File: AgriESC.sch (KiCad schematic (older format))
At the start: 131 parts, among them J1 SUPPLY, J10 GPIO, J11 USB_OTG, J12 HALL_ENC, J2 PH_A, J3 PH_B, J4 PH_C, J6 COMM, J7 SERVO, J8 CAN, J9 SWD, SW1 SW_SPDT, U1 FDMS7698, U10 STM32F405RGT6, U11 DRV8303, U12 TJA1051TK-3, U13 LMR16006YQ, U14 MCP1700-3302E_SOT23, U15 MCP1700-3302E_SOT23, U2 FDMS7698, U3 FDMS7698, U4 FDMS7698, U5 FDMS7698, U6 FDMS7698, U7 MAX9920, U8 MAX9920, U9 MAX9920, Y1 8M Resonator

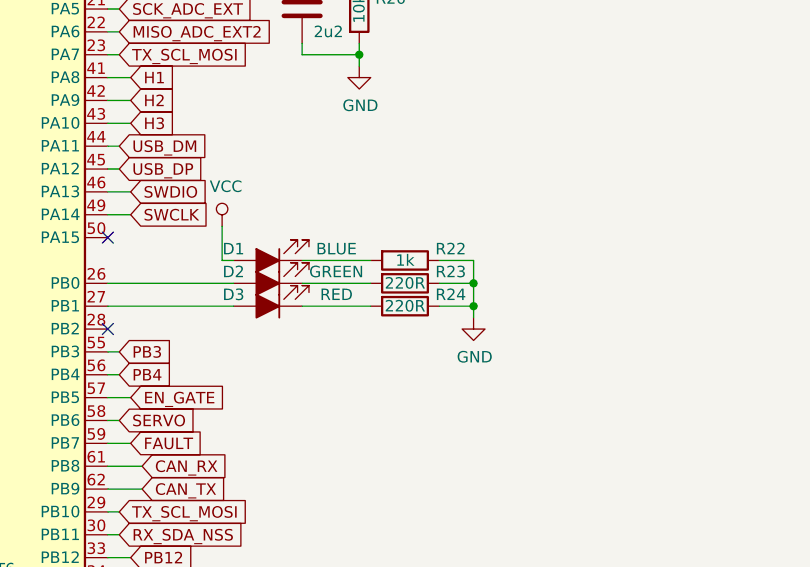
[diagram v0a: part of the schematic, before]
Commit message: Updated LED resistors
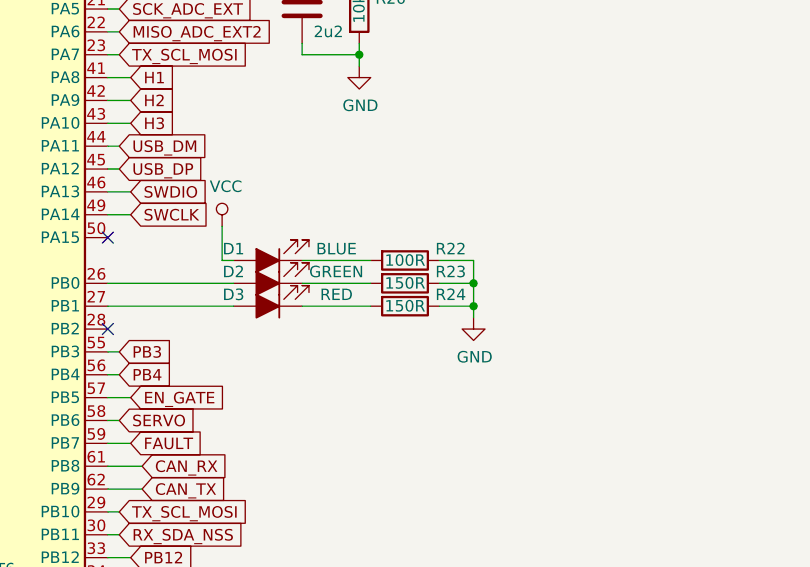
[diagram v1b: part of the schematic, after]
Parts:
- R22: value 1k -> 100R
- R23, R24: value 220R -> 150R
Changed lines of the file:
@@
 P 16400 7350
 F 0 "R22" V 16350 7550 50  0000 C CNN
-F 1 "1k" V 16400 7350 50  0000 C CNN
+F 1 "100R" V 16400 7350 50  0000 C CNN
 F 2 "Resistor_SMD:R_0603_1608Metric_Pad1.05x0.95mm_HandSolder" V 16330 7350 50  0001 C CNN
 F 3 "~" H 16400 7350 50  0001 C CNN
@@
 P 16400 7450
 F 0 "R23" V 16350 7650 50  0000 C CNN
-F 1 "220R" V 16400 7450 50  0000 C CNN
+F 1 "150R" V 16400 7450 50  0000 C CNN
 F 2 "Resistor_SMD:R_0603_1608Metric_Pad1.05x0.95mm_HandSolder" V 16330 7450 50  0001 C CNN
 F 3 "~" H 16400 7450 50  0001 C CNN
@@
 P 16400 7550
 F 0 "R24" V 16350 7750 50  0000 C CNN
-F 1 "220R" V 16400 7550 50  0000 C CNN
+F 1 "150R" V 16400 7550 50  0000 C CNN
 F 2 "Resistor_SMD:R_0603_1608Metric_Pad1.05x0.95mm_HandSolder" V 16330 7550 50  0001 C CNN
 F 3 "~" H 16400 7550 50  0001 C CNN

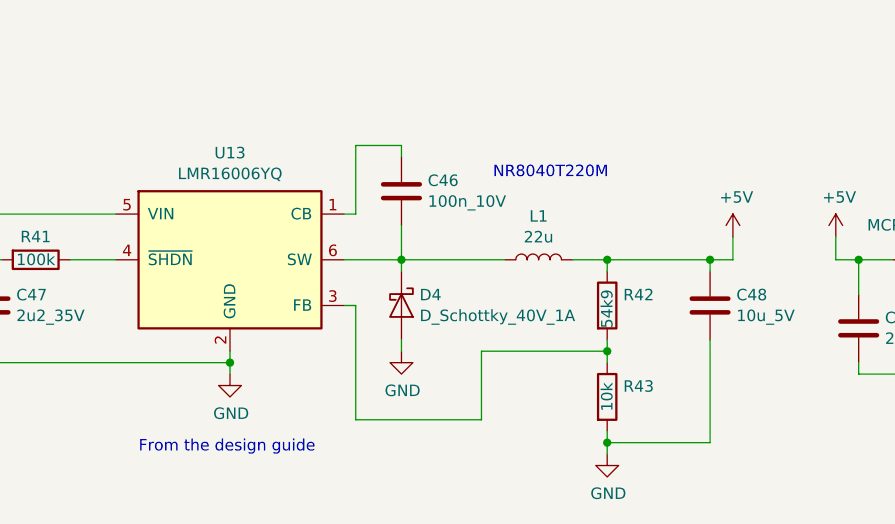
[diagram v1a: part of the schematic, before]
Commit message: Updated LMR16006YQ to fixed 5V version, removed feedback resistors
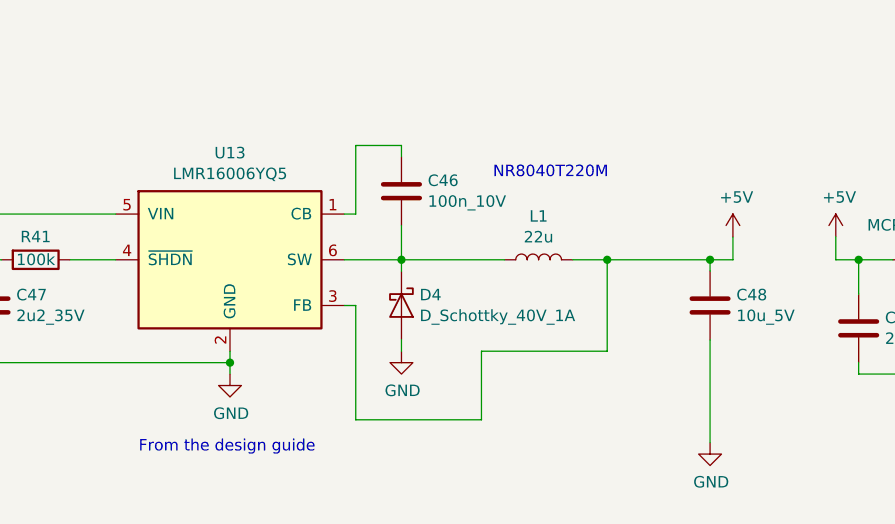
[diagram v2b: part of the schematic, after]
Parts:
- removed R42: 54k9, Resistor_SMD:R_0603_1608Metric_Pad1.05x0.95mm_HandSolder, symbol Device:R
- removed R43: 10k, Resistor_SMD:R_0603_1608Metric_Pad1.05x0.95mm_HandSolder, symbol Device:R
- U13: value LMR16006YQ -> LMR16006YQ5
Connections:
- net +5V: now also U13.3 (FB)
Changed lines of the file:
@@
 P 8700 13200
 F 0 "U13" H 8700 13667 50  0000 C CNN
-F 1 "LMR16006YQ" H 8700 13576 50  0000 C CNN
+F 1 "LMR16006YQ5" H 8700 13576 50  0000 C CNN
 F 2 "Package_TO_SOT_SMD:SOT-23-6" H 8700 12700 50  0001 C CIN
 F 3 "http://www.ti.com/lit/ds/symlink/lmr16006y-q1.pdf" H 8300 13650 50  0001 C CNN
@@
 	9450 13550 9450 13600
 $Comp
-L Device:R R42
-U 1 1 5DD532F3
-P 10350 13400
-F 0 "R42" H 10420 13446 50  0000 L CNN
-F 1 "54k9" V 10350 13300 50  0000 L CNN
-F 2 "Resistor_SMD:R_0603_1608Metric_Pad1.05x0.95mm_HandSolder" V 10280 13400 50  0001 C CNN
-F 3 "~" H 10350 13400 50  0001 C CNN
-	1    10350 13400
-	1    0    0    -1
-$EndComp
-$Comp
-L Device:R R43
-U 1 1 5DD53451
-P 10350 13800
-F 0 "R43" H 10420 13846 50  0000 L CNN
-F 1 "10k" V 10350 13800 50  0000 C CNN
-F 2 "Resistor_SMD:R_0603_1608Metric_Pad1.05x0.95mm_HandSolder" V 10280 13800 50  0001 C CNN
-F 3 "~" H 10350 13800 50  0001 C CNN
-	1    10350 13800
-	1    0    0    -1
-$EndComp
-$Comp
 L power:GND #PWR069
 U 1 1 5DD5355D
-P 10350 14050
-F 0 "#PWR069" H 10350 13800 50  0001 C CNN
-F 1 "GND" H 10355 13877 50  0000 C CNN
-F 2 "" H 10350 14050 50  0001 C CNN
-F 3 "" H 10350 14050 50  0001 C CNN
-	1    10350 14050
-	1    0    0    -1
-$EndComp
-Wire Wire Line
-	10350 13550 10350 13600
-Wire Wire Line
-	10350 13250 10350 13200
+P 10800 14000
+F 0 "#PWR069" H 10800 13750 50  0001 C CNN
+F 1 "GND" H 10805 13827 50  0000 C CNN
+F 2 "" H 10800 14000 50  0001 C CNN
+F 3 "" H 10800 14000 50  0001 C CNN
+	1    10800 14000
+	1    0    0    -1
+$EndComp
 Wire Wire Line
 	10350 13200 10200 13200
@@
 Wire Wire Line
 	9800 13600 10350 13600
-Connection ~ 10350 13600
-Wire Wire Line
-	10350 13600 10350 13650
 $Comp
 L Device:C C48
@@
 Wire Wire Line
 	10800 13550 10800 14000
-Wire Wire Line
-	10350 13950 10350 14000
-Wire Wire Line
-	10800 14000 10350 14000
-Connection ~ 10350 14000
-Wire Wire Line
-	10350 14000 10350 14050
 Wire Wire Line
 	10800 13200 10900 13200
@@
 Text Label 10050 10500 2    50   ~ 0
 HALL_POWER
+Wire Wire Line
+	10350 13200 10350 13600
 $EndSCHEMATC

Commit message: Updated USB footprint
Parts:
- J11: footprint AgriESC:CONN-10118194-0001LF-FCI2 -> AgriESC:CONN-10118194-0001LF-FCI3
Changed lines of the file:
@@
 F 0 "J11" H 15655 10267 50  0000 C CNN
 F 1 "USB_OTG" H 15655 10176 50  0000 C CNN
-F 2 "AgriESC:CONN-10118194-0001LF-FCI2" H 15750 9750 50  0001 C CNN
+F 2 "AgriESC:CONN-10118194-0001LF-FCI3" H 15750 9750 50  0001 C CNN
 F 3 " ~" H 15750 9750 50  0001 C CNN
 	1    15600 9800

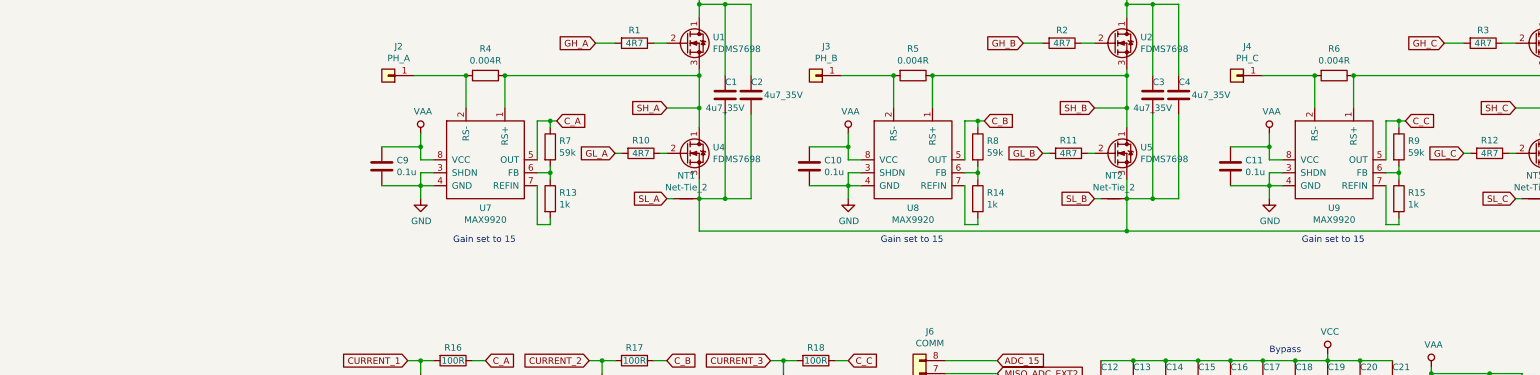
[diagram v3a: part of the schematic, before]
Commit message: Added new MAX9920 VREFIN
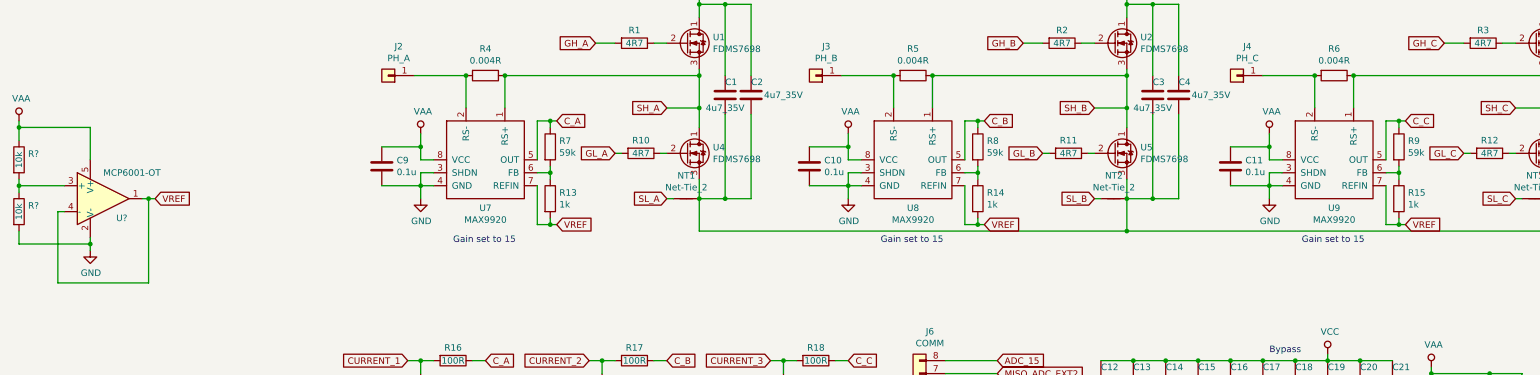
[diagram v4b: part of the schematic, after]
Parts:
- added R? (x2): 10k, Resistor_SMD:R_0603_1608Metric_Pad1.05x0.95mm_HandSolder, symbol Device:R
- added U?: MCP6001-OT, Package_TO_SOT_SMD:SOT-23-5, symbol Amplifier_Operational:MCP6001-OT
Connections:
- net GND: now also R?.2, U?.2 (V-)
- net VAA: now also R?.1, U?.5 (V+)
- net VREF: now reaches R13.2, U7.7 (REFIN)
- net VREF: now also R14.2, R15.2, U8.7 (REFIN), U9.7 (REFIN), U?.1, U?.4 (-)
- new net: R?.1, R?.2, U?.3 (+)
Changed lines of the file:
@@
 EESchema Schematic File Version 4
 LIBS:AgriESC-cache
-EELAYER 26 0
+EELAYER 29 0
 EELAYER END
 $Descr A2 23386 16535
@@
 Wire Wire Line
 	10350 13200 10350 13600
+$Comp
+L Amplifier_Operational:MCP6001-OT U?
+U 1 1 5CA0408E
+P 4450 3700
+F 0 "U?" H 4550 3550 50  0000 L CNN
+F 1 "MCP6001-OT" H 4450 3900 50  0000 L CNN
+F 2 "Package_TO_SOT_SMD:SOT-23-5" H 4350 3500 50  0001 L CNN
+F 3 "http://ww1.microchip.com/downloads/en/DeviceDoc/21733j.pdf" H 4450 3900 50  0001 C CNN
+	1    4450 3700
+	1    0    0    -1
+$EndComp
+$Comp
+L power:GND #PWR?
+U 1 1 5CA05164
+P 4350 4100
+F 0 "#PWR?" H 4350 3850 50  0001 C CNN
+F 1 "GND" H 4355 3927 50  0000 C CNN
+F 2 "" H 4350 4100 50  0001 C CNN
+F 3 "" H 4350 4100 50  0001 C CNN
+	1    4350 4100
+	1    0    0    -1
+$EndComp
+Wire Wire Line
+	4350 4000 4350 4050
+Wire Wire Line
+	4800 4350 4800 3700
+Wire Wire Line
+	4800 3700 4750 3700
+Wire Wire Line
+	4100 4350 4800 4350
+Wire Wire Line
+	4150 3800 4100 3800
+Wire Wire Line
+	4100 3800 4100 4350
+$Comp
+L Device:R R?
+U 1 1 5CC894C1
+P 3800 3400
+F 0 "R?" H 3870 3446 50  0000 L CNN
+F 1 "10k" V 3800 3400 50  0000 C CNN
+F 2 "Resistor_SMD:R_0603_1608Metric_Pad1.05x0.95mm_HandSolder" V 3730 3400 50  0001 C CNN
+F 3 "~" H 3800 3400 50  0001 C CNN
+	1    3800 3400
+	1    0    0    -1
+$EndComp
+$Comp
+L Device:R R?
+U 1 1 5CC902E6
+P 3800 3800
+F 0 "R?" H 3870 3846 50  0000 L CNN
+F 1 "10k" V 3800 3800 50  0000 C CNN
+F 2 "Resistor_SMD:R_0603_1608Metric_Pad1.05x0.95mm_HandSolder" V 3730 3800 50  0001 C CNN
+F 3 "~" H 3800 3800 50  0001 C CNN
+	1    3800 3800
+	1    0    0    -1
+$EndComp
+Wire Wire Line
+	3800 3550 3800 3600
+Wire Wire Line
+	4150 3600 3800 3600
+Connection ~ 3800 3600
+Wire Wire Line
+	3800 3600 3800 3650
+Wire Wire Line
+	3800 3250 3800 3150
+Wire Wire Line
+	3800 3150 4350 3150
+Wire Wire Line
+	4350 3150 4350 3400
+Wire Wire Line
+	4800 3700 4850 3700
+Connection ~ 4800 3700
+Wire Wire Line
+	4350 4050 3800 4050
+Wire Wire Line
+	3800 4050 3800 3950
+Connection ~ 4350 4050
+Wire Wire Line
+	4350 4050 4350 4100
+Wire Wire Line
+	3800 3150 3800 3100
+Connection ~ 3800 3150
+Text GLabel 4850 3700 2    50   Input ~ 0
+VREF
+$Comp
+L power:VAA #PWR?
+U 1 1 5D069BCC
+P 3800 3100
+F 0 "#PWR?" H 3800 2950 50  0001 C CNN
+F 1 "VAA" H 3817 3273 50  0000 C CNN
+F 2 "" H 3800 3100 50  0001 C CNN
+F 3 "" H 3800 3100 50  0001 C CNN
+	1    3800 3100
+	1    0    0    -1
+$EndComp
+Text GLabel 7950 3900 2    50   Input ~ 0
+VREF
+Wire Wire Line
+	7950 3900 7900 3900
+Connection ~ 7900 3900
+Text GLabel 11250 3900 2    50   Input ~ 0
+VREF
+Wire Wire Line
+	11250 3900 11200 3900
+Connection ~ 11200 3900
+Text GLabel 14500 3900 2    50   Input ~ 0
+VREF
+Wire Wire Line
+	14500 3900 14450 3900
+Connection ~ 14450 3900
 $EndSCHEMATC

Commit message: Annotations
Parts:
- gave numbers to parts that had none: 3
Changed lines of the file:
@@
 	10350 13200 10350 13600
 $Comp
-L Amplifier_Operational:MCP6001-OT U?
+L Amplifier_Operational:MCP6001-OT U16
 U 1 1 5CA0408E
 P 4450 3700
-F 0 "U?" H 4550 3550 50  0000 L CNN
+F 0 "U16" H 4550 3550 50  0000 L CNN
 F 1 "MCP6001-OT" H 4450 3900 50  0000 L CNN
 F 2 "Package_TO_SOT_SMD:SOT-23-5" H 4350 3500 50  0001 L CNN
@@
 $EndComp
 $Comp
-L power:GND #PWR?
+L power:GND #PWR070
 U 1 1 5CA05164
 P 4350 4100
-F 0 "#PWR?" H 4350 3850 50  0001 C CNN
+F 0 "#PWR070" H 4350 3850 50  0001 C CNN
 F 1 "GND" H 4355 3927 50  0000 C CNN
 F 2 "" H 4350 4100 50  0001 C CNN
@@
 	4100 3800 4100 4350
 $Comp
-L Device:R R?
+L Device:R R42
 U 1 1 5CC894C1
 P 3800 3400
-F 0 "R?" H 3870 3446 50  0000 L CNN
+F 0 "R42" H 3870 3446 50  0000 L CNN
 F 1 "10k" V 3800 3400 50  0000 C CNN
 F 2 "Resistor_SMD:R_0603_1608Metric_Pad1.05x0.95mm_HandSolder" V 3730 3400 50  0001 C CNN
@@
 $EndComp
 $Comp
-L Device:R R?
+L Device:R R43
 U 1 1 5CC902E6
 P 3800 3800
-F 0 "R?" H 3870 3846 50  0000 L CNN
+F 0 "R43" H 3870 3846 50  0000 L CNN
 F 1 "10k" V 3800 3800 50  0000 C CNN
 F 2 "Resistor_SMD:R_0603_1608Metric_Pad1.05x0.95mm_HandSolder" V 3730 3800 50  0001 C CNN
@@
 VREF
 $Comp
-L power:VAA #PWR?
+L power:VAA #PWR032
 U 1 1 5D069BCC
 P 3800 3100
-F 0 "#PWR?" H 3800 2950 50  0001 C CNN
+F 0 "#PWR032" H 3800 2950 50  0001 C CNN
 F 1 "VAA" H 3817 3273 50  0000 C CNN
 F 2 "" H 3800 3100 50  0001 C CNN
